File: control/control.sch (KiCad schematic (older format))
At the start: 82 parts, among them M1 LMR62014, M2 LM46001, M3 STM32F4XX, M4 TPS736XX, M5 SN65HVD23X, P1 PLS_2, P2 PLS_4, P3 PLS_4, P4 PLS_10, P5 PLS_3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

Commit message: Added OpAmp buffer, a lot of small fixes.
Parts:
- added C44: 120pF, foot:SM0603, symbol C
- added C45: 100nF, foot:SM0603, symbol C
- added P8: PLS_1, foot:PLS1, symbol PLS_1
- added R14: 470K 1%, foot:SM0603, symbol R
- added R15: 27K 1%, foot:SM0603, symbol R
- added U1: AD8539, foot:MSOP8, symbol AD8539
- C36: value 1nF -> 120pF
- R16: value 47K 1% -> 470K 1%
- R17: value 2K7 1% -> 27K 1%
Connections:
- net labels added: ADC_IN12, ADC_IN13, HVIN
- wire segments 215 -> 238
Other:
- moved on the sheet: C1, C10, C11, C12, C13, C14, C15, C16, C17, C18, C19, C2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

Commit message: Added encoder inputs on control board, removed SWD, changed USART.
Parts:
- removed P2, P3: PLS_4, foot:PLS4, symbol PLS_4
- removed P8: PLS_1, foot:PLS1, symbol PLS_1
- removed R10, R12, R13, R9: 47, foot:SM0603, symbol R
- added P2: PLS_2, foot:PLS2, symbol PLS_2
- added P3: PLS_8, foot:PLS8, symbol PLS_8
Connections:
- net labels added: BOOT, EN_A, EN_B, USART_RX, USART_TX
- wire segments 238 -> 235

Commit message: Added DAC outputs, SWD outputs, fixes.
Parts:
- added P8: SWD, foot:PLS2, symbol PLS_2
- added R10, R9: 10K, foot:SM0603, symbol R
- P1: value PLS_2 -> ENCODER
- P2: value PLS_2 -> VOLTAGE
- P3: value PLS_8 -> CONTROL
- P4: value PLS_10 -> POWER
- P5, P6: value PLS_3 -> SENSOR
- P7: value PLS_2 -> CAN
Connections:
- net +3.3V: now also R10.2, R9.2; no longer P3.6
- net BOOT: now also P3.7; no longer P3.5
- net EN_A: now also R9.1
- net EN_B: now also R10.1
- net GND: no longer P3.8
- net NRST: now also P3.8; no longer P3.7
- net DAC_OUT1: now reaches M3.20 (PA4/DAC_OUT1)
- net DAC_OUT1: now also P3.6
- net DAC_OUT2: now reaches M3.21 (PA5/DAC_OUT2)
- net DAC_OUT2: now also P3.5
- net at M3.46 (PA13/SWDIO): now also P8.1
- net at M3.49 (PA14/SWDCLK): now also P8.2

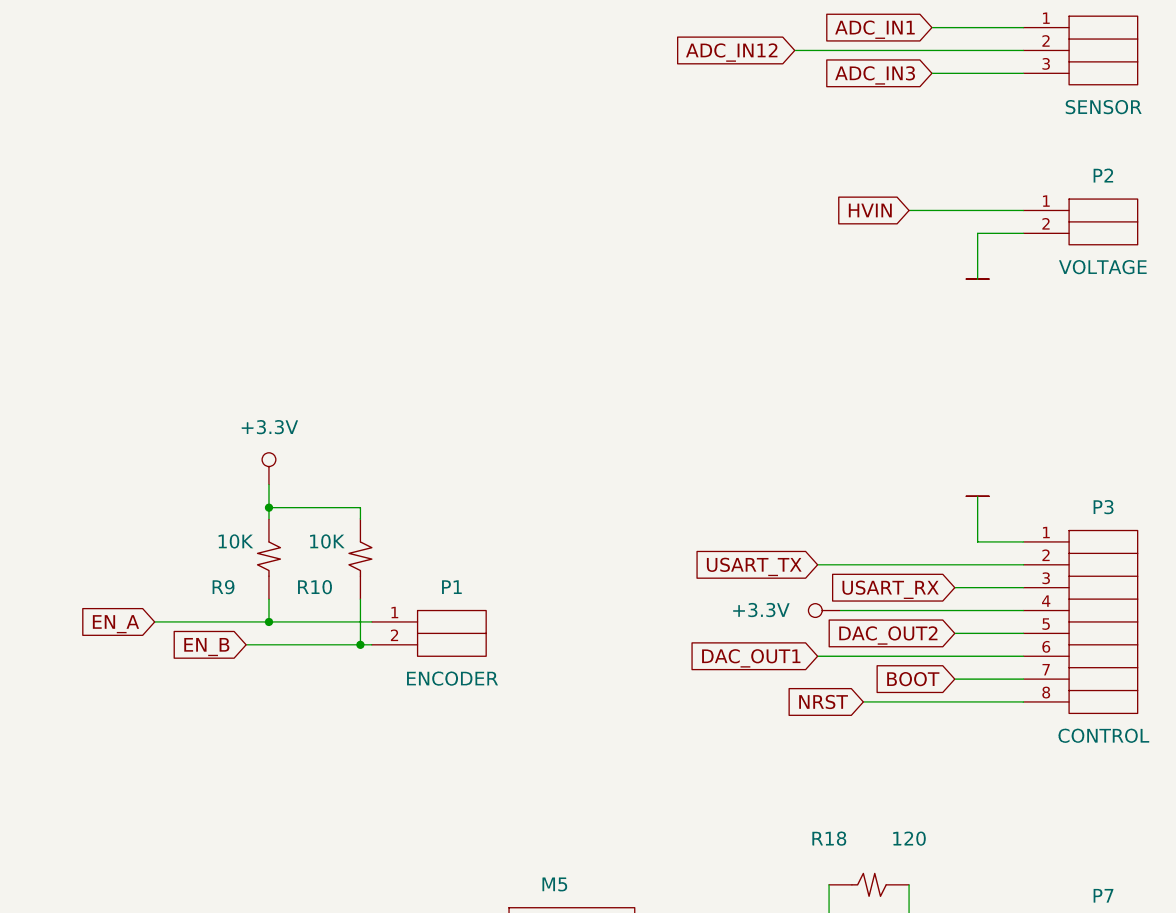
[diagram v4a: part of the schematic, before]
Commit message: Added jumper outputs.
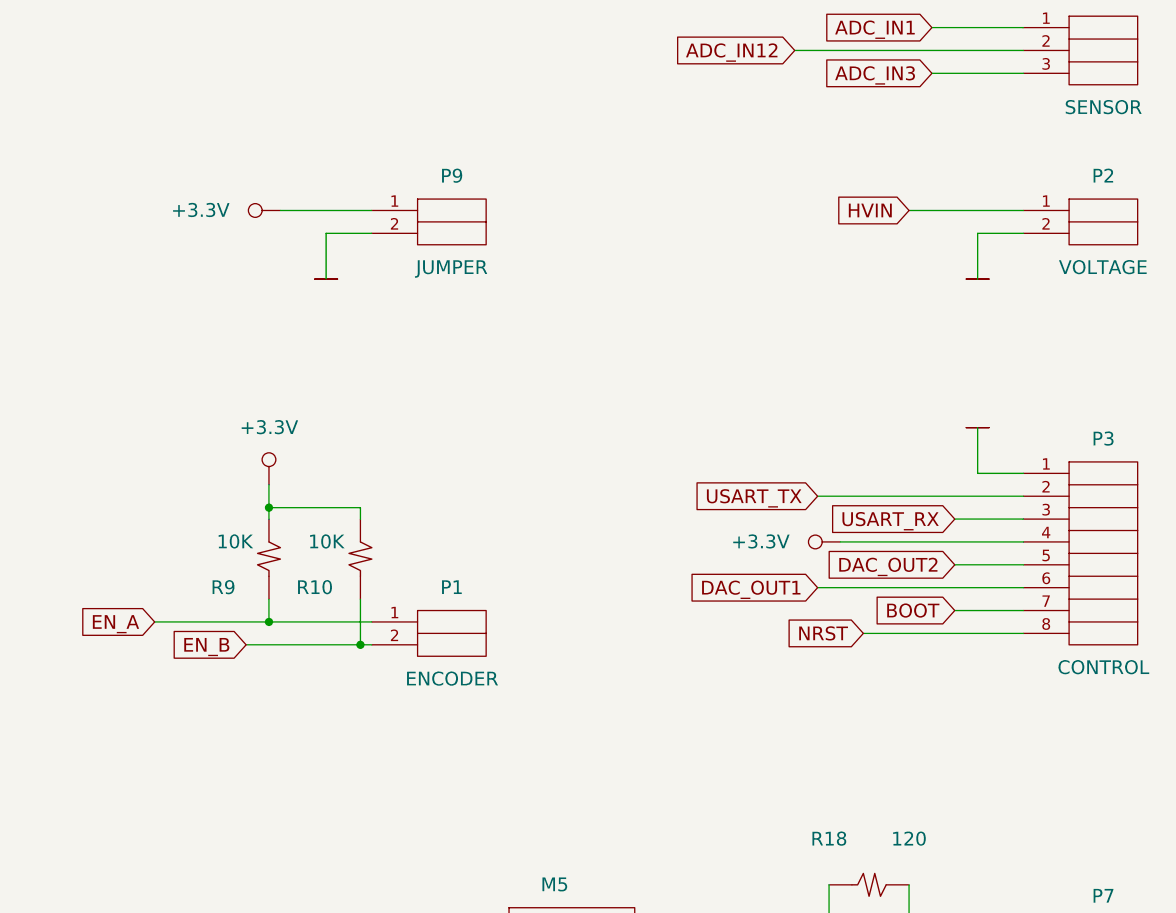
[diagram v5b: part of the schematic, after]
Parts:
- added P9: JUMPER, foot:PLS2, symbol PLS_2
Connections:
- net +3.3V: now also P9.1
- net GND: now also P9.2
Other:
- moved on the sheet: P3
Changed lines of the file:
@@
 $EndComp
 $Comp
-L GND #PWR48
+L GND #PWR50
 U 1 1 5686AEC1
 P 14800 2500
-F 0 "#PWR48" H 14800 2500 30  0001 C CNN
+F 0 "#PWR50" H 14800 2500 30  0001 C CNN
 F 1 "GND" H 14800 2430 30  0001 C CNN
 F 2 "" H 14800 2500 60  0000 C CNN
@@
 $EndComp
 $Comp
-L GND #PWR43
+L GND #PWR45
 U 1 1 5686AEC2
 P 13900 3100
-F 0 "#PWR43" H 13900 3100 30  0001 C CNN
+F 0 "#PWR45" H 13900 3100 30  0001 C CNN
 F 1 "GND" H 13900 3030 30  0001 C CNN
 F 2 "" H 13900 3100 60  0000 C CNN
@@
 $EndComp
 $Comp
-L +12V #PWR44
+L +12V #PWR46
 U 1 1 5686AED6
 P 14150 2100
-F 0 "#PWR44" H 14150 2190 20  0001 C CNN
+F 0 "#PWR46" H 14150 2190 20  0001 C CNN
 F 1 "+12V" V 14150 2450 60  0000 C CNN
 F 2 "" H 14150 2100 60  0000 C CNN
@@
 CAN_TX
 $Comp
-L +3.3V #PWR38
+L +3.3V #PWR39
 U 1 1 5686AF19
 P 11950 8950
-F 0 "#PWR38" H 11950 9040 20  0001 C CNN
+F 0 "#PWR39" H 11950 9040 20  0001 C CNN
 F 1 "+3.3V" V 11950 9300 60  0000 C CNN
 F 2 "" H 11950 8950 60  0000 C CNN
@@
 $EndComp
 $Comp
-L GND #PWR41
+L GND #PWR43
 U 1 1 5686AF1A
 P 12600 9300
-F 0 "#PWR41" H 12600 9300 30  0001 C CNN
+F 0 "#PWR43" H 12600 9300 30  0001 C CNN
 F 1 "GND" H 12600 9230 30  0001 C CNN
 F 2 "" H 12600 9300 60  0000 C CNN
@@
 $EndComp
 $Comp
-L GND #PWR42
+L GND #PWR44
 U 1 1 5686AF1F
 P 13650 8600
-F 0 "#PWR42" H 13650 8600 30  0001 C CNN
+F 0 "#PWR44" H 13650 8600 30  0001 C CNN
 F 1 "GND" H 13650 8530 30  0001 C CNN
 F 2 "" H 13650 8600 60  0000 C CNN
@@
 FET_BL
 $Comp
-L +36V #PWR46
+L +36V #PWR48
 U 1 1 5692B58F
 P 14450 1100
-F 0 "#PWR46" H 14450 1190 20  0001 C CNN
+F 0 "#PWR48" H 14450 1190 20  0001 C CNN
 F 1 "+36V" H 14440 1300 60  0000 C CNN
 F 2 "" H 14450 1100 60  0000 C CNN
@@
 NRST
 $Comp
-L +3.3V #PWR47
+L +3.3V #PWR49
 U 1 1 5699D8BB
 P 14650 3200
-F 0 "#PWR47" H 14650 3290 20  0001 C CNN
+F 0 "#PWR49" H 14650 3290 20  0001 C CNN
 F 1 "+3.3V" V 14650 3550 60  0000 C CNN
 F 2 "" H 14650 3200 60  0000 C CNN
@@
 $EndComp
 $Comp
-L +3.3V #PWR40
+L +3.3V #PWR42
 U 1 1 56B91810
 P 12100 2550
-F 0 "#PWR40" H 12100 2640 20  0001 C CNN
+F 0 "#PWR42" H 12100 2640 20  0001 C CNN
 F 1 "+3.3V" V 12100 2900 60  0000 C CNN
 F 2 "" H 12100 2550 60  0000 C CNN
@@
 $EndComp
 $Comp
-L +3.3V #PWR39
+L +3.3V #PWR41
 U 1 1 56B94566
 P 12100 1200
-F 0 "#PWR39" H 12100 1290 20  0001 C CNN
+F 0 "#PWR41" H 12100 1290 20  0001 C CNN
 F 1 "+3.3V" V 12100 1550 60  0000 C CNN
 F 2 "" H 12100 1200 60  0000 C CNN
@@
 ADC_IN12
 $Comp
-L GND #PWR49
+L GND #PWR51
 U 1 1 56C66181
 P 14850 5000
-F 0 "#PWR49" H 14850 5000 30  0001 C CNN
+F 0 "#PWR51" H 14850 5000 30  0001 C CNN
 F 1 "GND" H 14850 4930 30  0001 C CNN
 F 2 "" H 14850 5000 60  0000 C CNN
@@
 L PLS_8 P3
 U 1 1 56C300F1
-P 15400 6500
-F 0 "P3" H 15400 7000 60  0000 C CNN
-F 1 "CONTROL" H 15400 6000 60  0000 C CNN
-F 2 "foot:PLS8" H 15050 6000 60  0001 C CNN
-F 3 "" H 15550 6450 60  0000 C CNN
-	1    15400 6500
-	1    0    0    -1
-$EndComp
-$Comp
-L GND #PWR50
+P 15400 6200
+F 0 "P3" H 15400 6700 60  0000 C CNN
+F 1 "CONTROL" H 15400 5700 60  0000 C CNN
+F 2 "foot:PLS8" H 15050 5700 60  0001 C CNN
+F 3 "" H 15550 6150 60  0000 C CNN
+	1    15400 6200
+	1    0    0    -1
+$EndComp
+$Comp
+L GND #PWR52
 U 1 1 56C30536
-P 14850 5950
-F 0 "#PWR50" H 14850 5950 30  0001 C CNN
-F 1 "GND" H 14850 5880 30  0001 C CNN
-F 2 "" H 14850 5950 60  0000 C CNN
-F 3 "" H 14850 5950 60  0000 C CNN
-	1    14850 5950
-	1    0    0    -1
-$EndComp
-$Comp
-L +3.3V #PWR45
+P 14850 5650
+F 0 "#PWR52" H 14850 5650 30  0001 C CNN
+F 1 "GND" H 14850 5580 30  0001 C CNN
+F 2 "" H 14850 5650 60  0000 C CNN
+F 3 "" H 14850 5650 60  0000 C CNN
+	1    14850 5650
+	1    0    0    -1
+$EndComp
+$Comp
+L +3.3V #PWR47
 U 1 1 56C3064F
-P 14250 6450
-F 0 "#PWR45" H 14250 6540 20  0001 C CNN
-F 1 "+3.3V" V 14250 6800 60  0000 C CNN
-F 2 "" H 14250 6450 60  0000 C CNN
-F 3 "" H 14250 6450 60  0000 C CNN
-	1    14250 6450
-	0    -1   -1   0
-$EndComp
-Text GLabel 14350 6850 0    60   Input ~ 0
+P 14250 6150
+F 0 "#PWR47" H 14250 6240 20  0001 C CNN
+F 1 "+3.3V" V 14250 6500 60  0000 C CNN
+F 2 "" H 14250 6150 60  0000 C CNN
+F 3 "" H 14250 6150 60  0000 C CNN
+	1    14250 6150
+	0    -1   -1   0
+$EndComp
+Text GLabel 14350 6550 0    60   Input ~ 0
 NRST
 Text GLabel 9050 9900 2    60   Input ~ 0
@@
 Wire Wire Line
 	8300 9900 9050 9900
-Text GLabel 14750 6750 0    60   Input ~ 0
+Text GLabel 14750 6450 0    60   Input ~ 0
 BOOT
 Wire Wire Line
-	14250 6450 15050 6450
+	14250 6150 15050 6150
 Text GLabel 8550 8800 2    60   Input ~ 0
 USART_TX
@@
 	1    0    0    -1
 $EndComp
-Text GLabel 14150 6250 0    60   Input ~ 0
+Text GLabel 14150 5950 0    60   Input ~ 0
 USART_TX
-Text GLabel 14750 6350 0    60   Input ~ 0
+Text GLabel 14750 6050 0    60   Input ~ 0
 USART_RX
 Wire Wire Line
-	15050 6350 14750 6350
-Wire Wire Line
-	15050 6250 14150 6250
+	15050 6050 14750 6050
+Wire Wire Line
+	15050 5950 14150 5950
 Text GLabel 9500 7600 2    60   Input ~ 0
 EN_A
@@
 	6500 8300 5150 8300
 Wire Wire Line
-	15050 6150 14850 6150
-Wire Wire Line
-	14850 6150 14850 5950
-Text GLabel 14150 6650 0    60   Input ~ 0
+	15050 5850 14850 5850
+Wire Wire Line
+	14850 5850 14850 5650
+Text GLabel 14150 6350 0    60   Input ~ 0
 DAC_OUT1
-Text GLabel 14750 6550 0    60   Input ~ 0
+Text GLabel 14750 6250 0    60   Input ~ 0
 DAC_OUT2
 Wire Wire Line
-	14750 6550 15050 6550
-Wire Wire Line
-	15050 6650 14150 6650
-Wire Wire Line
-	14750 6750 15050 6750
-Wire Wire Line
-	15050 6850 14350 6850
+	14750 6250 15050 6250
+Wire Wire Line
+	15050 6350 14150 6350
+Wire Wire Line
+	14750 6450 15050 6450
+Wire Wire Line
+	15050 6550 14350 6550
 $Comp
 L PLS_2 P8
@@
 	12150 6000 11750 6000
 Connection ~ 11750 6000
+$Comp
+L PLS_2 P9
+U 1 1 56C3671A
+P 12550 4750
+F 0 "P9" H 12550 4950 60  0000 C CNN
+F 1 "JUMPER" H 12550 4550 60  0000 C CNN
+F 2 "foot:PLS2" H 12200 4500 60  0001 C CNN
+F 3 "" H 12700 4350 60  0000 C CNN
+	1    12550 4750
+	1    0    0    -1
+$EndComp
+$Comp
+L GND #PWR40
+U 1 1 56C386AD
+P 12000 5000
+F 0 "#PWR40" H 12000 5000 30  0001 C CNN
+F 1 "GND" H 12000 4930 30  0001 C CNN
+F 2 "" H 12000 5000 60  0000 C CNN
+F 3 "" H 12000 5000 60  0000 C CNN
+	1    12000 5000
+	1    0    0    -1
+$EndComp
+$Comp
+L +3.3V #PWR38
+U 1 1 56C39BB0
+P 11800 4700
+F 0 "#PWR38" H 11800 4790 20  0001 C CNN
+F 1 "+3.3V" V 11800 5050 60  0000 C CNN
+F 2 "" H 11800 4700 60  0000 C CNN
+F 3 "" H 11800 4700 60  0000 C CNN
+	1    11800 4700
+	0    -1   -1   0
+$EndComp
+Wire Wire Line
+	12000 5000 12000 4800
+Wire Wire Line
+	12000 4800 12200 4800
+Wire Wire Line
+	12200 4700 11800 4700
 $EndSCHEMATC

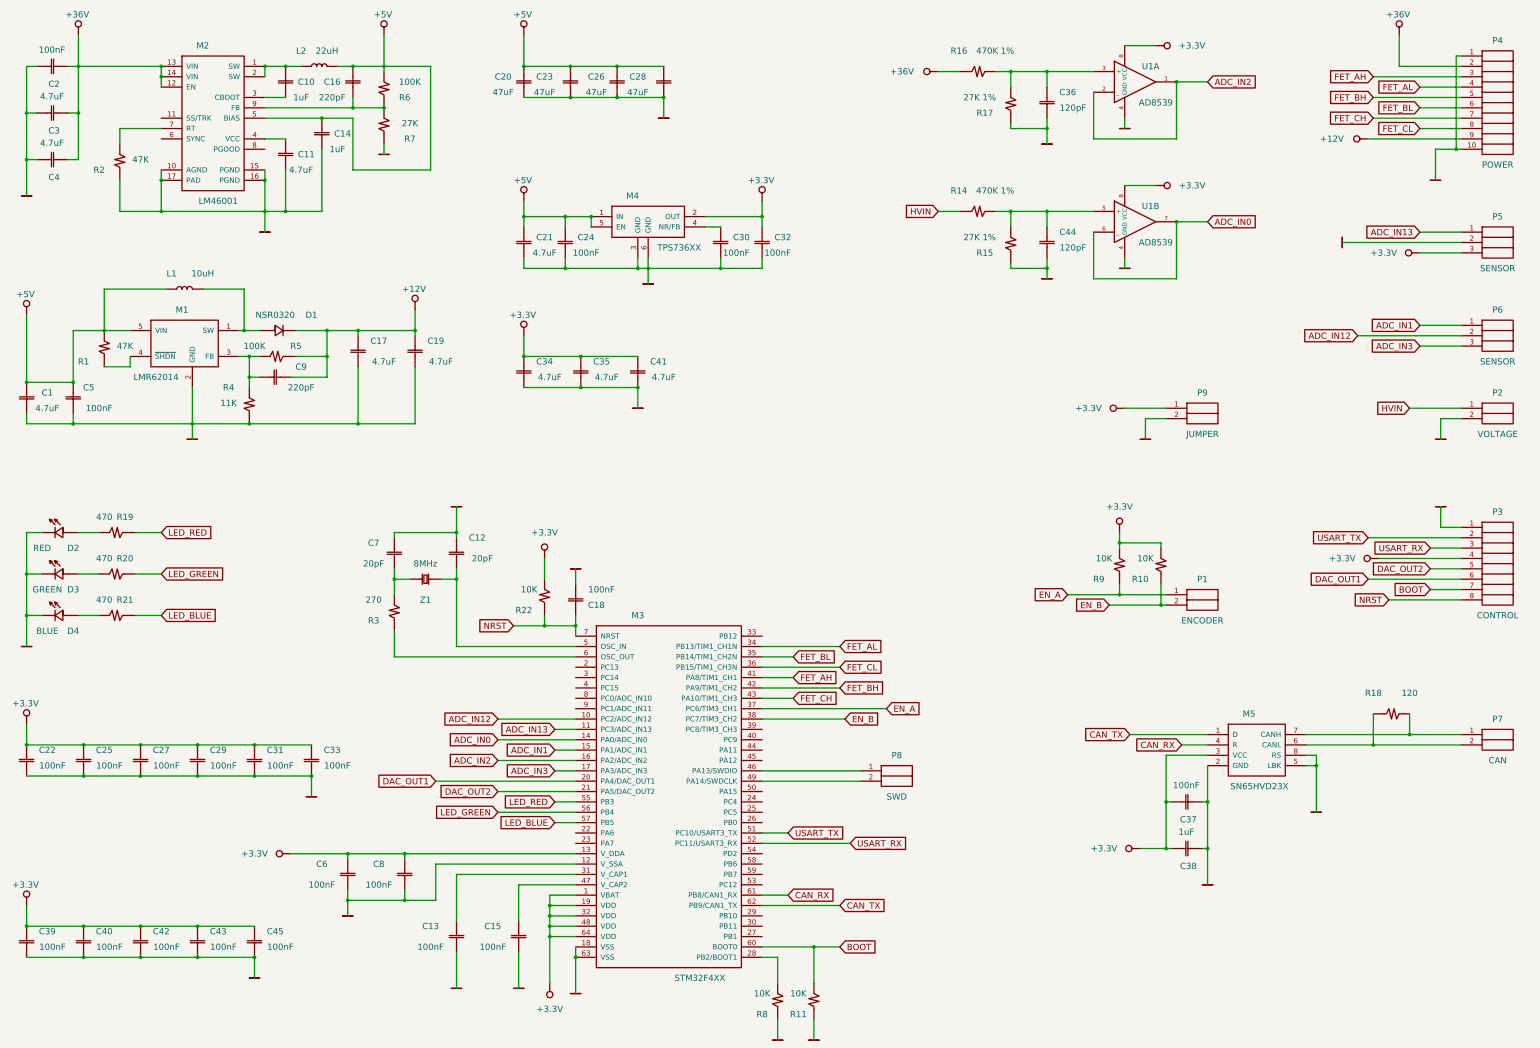
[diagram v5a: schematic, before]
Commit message: Accumulated changes, large track width, encoder/hall interface, etc.
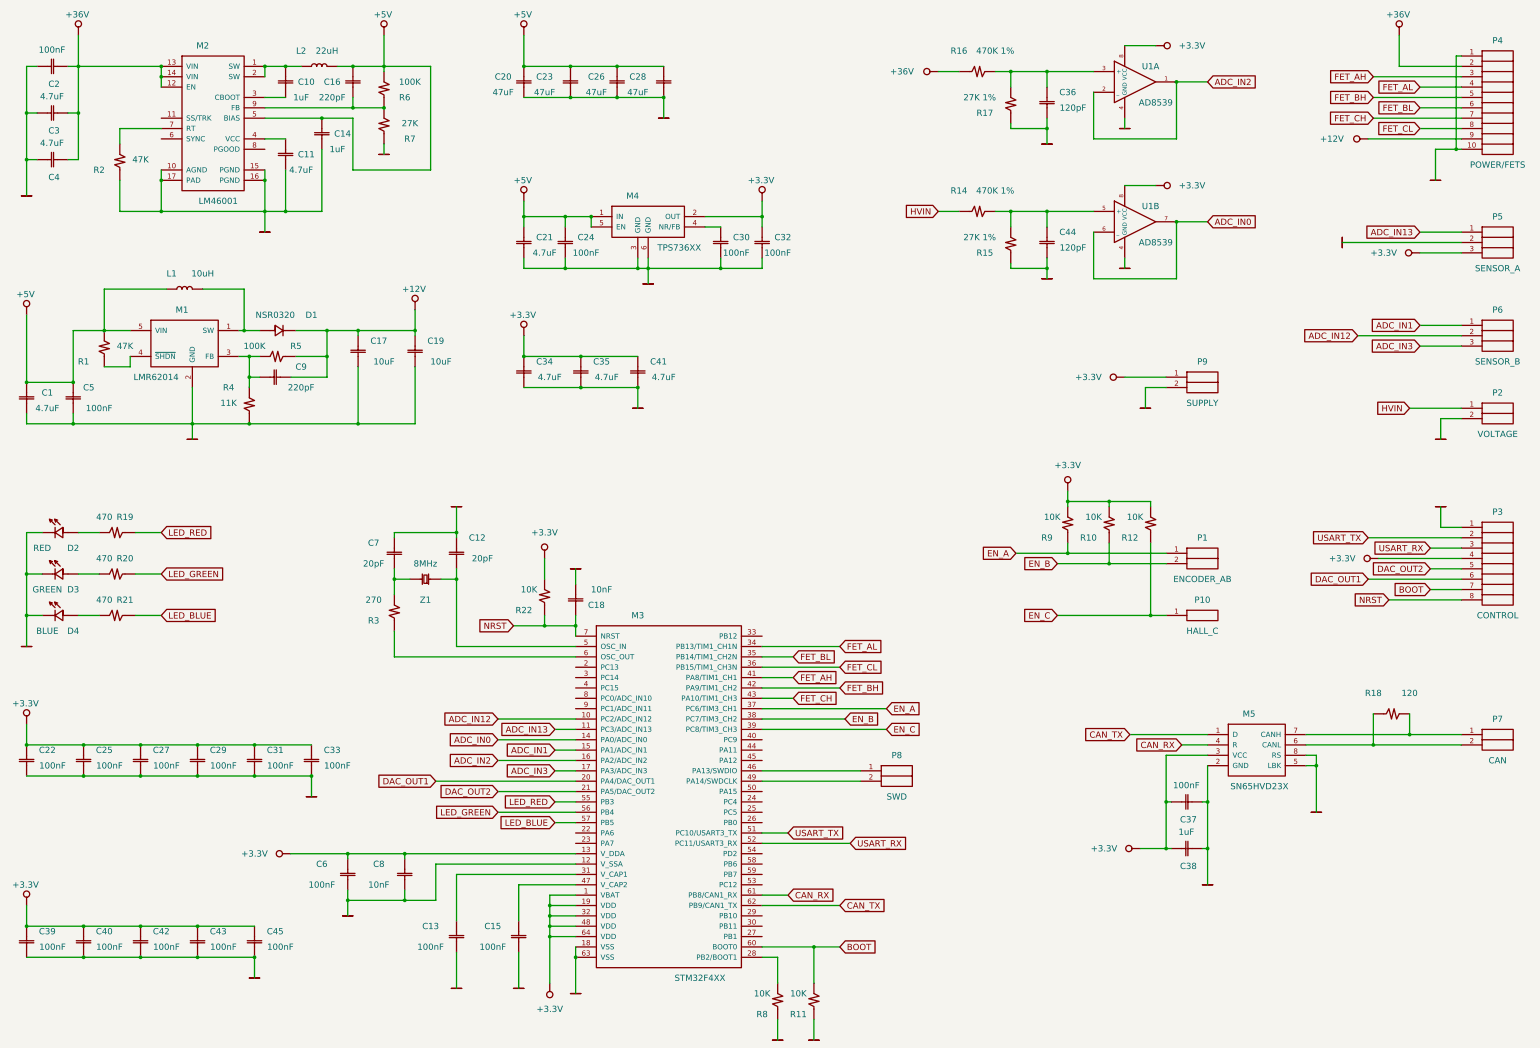
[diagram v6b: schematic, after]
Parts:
- added P10: HALL_C, foot:PLS1, symbol PLS_1
- added R12: 10K, foot:SM0603, symbol R
- C17, C19: value 4.7uF -> 10uF
- C18, C8: value 100nF -> 10nF
- P1: value ENCODER -> ENCODER_AB
- P4: value POWER -> POWER/FETS
- P5: value SENSOR -> SENSOR_A
- P6: value SENSOR -> SENSOR_B
- P9: value JUMPER -> SUPPLY
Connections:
- net +3.3V: now also R12.2
- net EN_C: now reaches M3.39 (PC8/TIM3_CH3)
- net EN_C: now also P10.1, R12.1
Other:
- moved on the sheet: P1, P9, R10, R9
